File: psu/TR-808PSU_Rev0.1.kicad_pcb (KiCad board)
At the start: 2 copper layers, 142.9 x 119.4 mm, 67 parts, among them IC1 uA7805, IC2 TA7179P, P1 1, P10 10, P11 11, P12 12, P13 13, P14 14, P15 15, P16 16, P17 17, P18 18, P19 19, P2 2, P20 20, P21 21, P22 22, P3 3, P4 4, P5 5, P6 6, P7 7, P8 8, P9 9, Q1 2SB596, Q2 2SD880

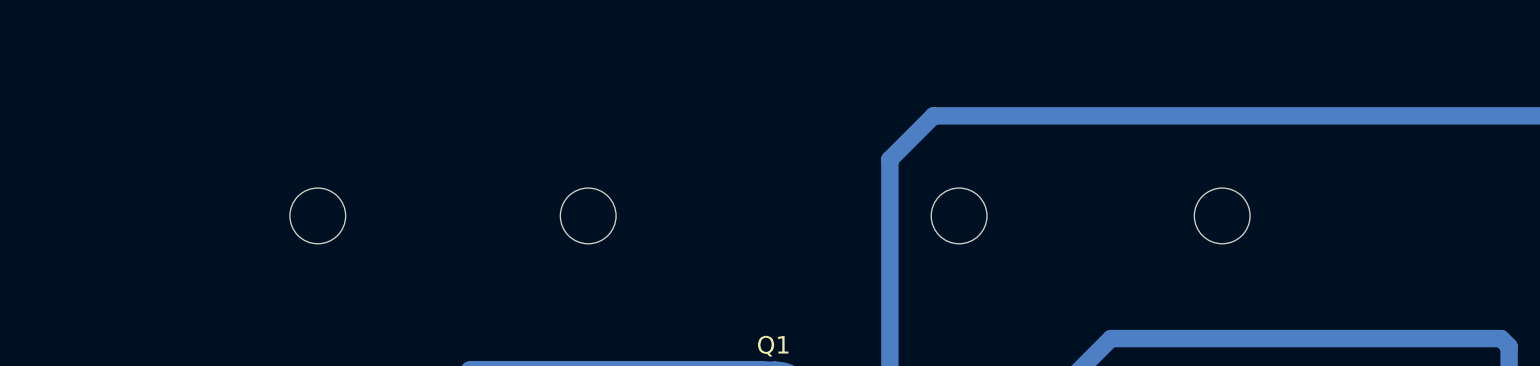
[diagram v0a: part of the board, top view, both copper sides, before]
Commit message: Schraubenloecher fuer IC1, Q1, Q2 (M3, H11-H13)
Auf der Mittelachse der Regler, 1,9 mm ueber den Seitenloechern (Bestueckungsplan).
Schaltplan mit 13 Befestigungsloechern, ERC 0, DRC 0 Fehler, Abgleich 0.

Co-Authored-By: Claude Sonnet 5.5 <noreply@anthropic.com>
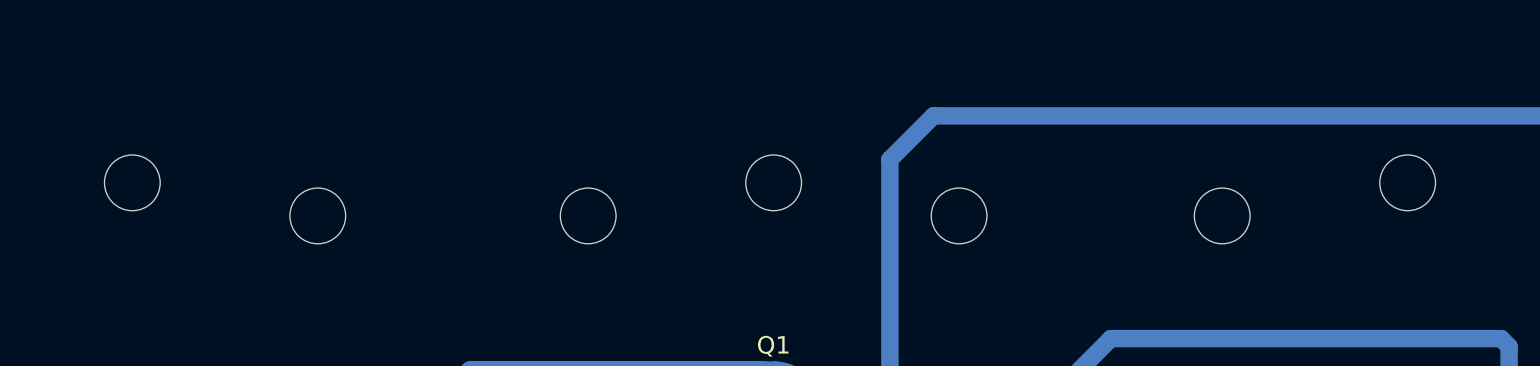
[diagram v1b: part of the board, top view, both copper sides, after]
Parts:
- added H11: M3, MountingHole:MountingHole_3.2mm_M3, F.Cu at (54.4, 32.7)
- added H12: M3, MountingHole:MountingHole_3.2mm_M3, F.Cu at (91.3, 32.7)
- added H13: M3, MountingHole:MountingHole_3.2mm_M3, F.Cu at (127.7, 32.7)

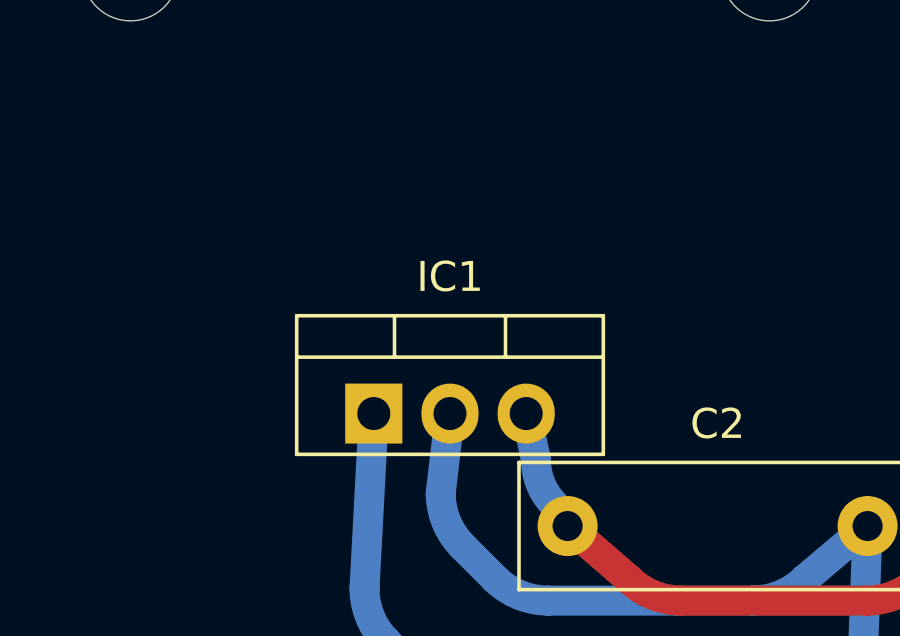
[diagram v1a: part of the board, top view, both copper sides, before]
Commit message: Regler auf einer Hoehe, Bruecken W04
IC1 auf die Hoehe von Q1/Q2 (y 47,135 mm), Bahnen ueber kurze Stuecke angebunden. D1/D2 als W04
(Platine: 2W04G; Manual W-02). Schaltplan, Stueckliste, Gerber, Ausdruck neu. ERC 0, DRC 0 Fehler, Abgleich 0.

Co-Authored-By: Claude Sonnet 5.5 <noreply@anthropic.com>
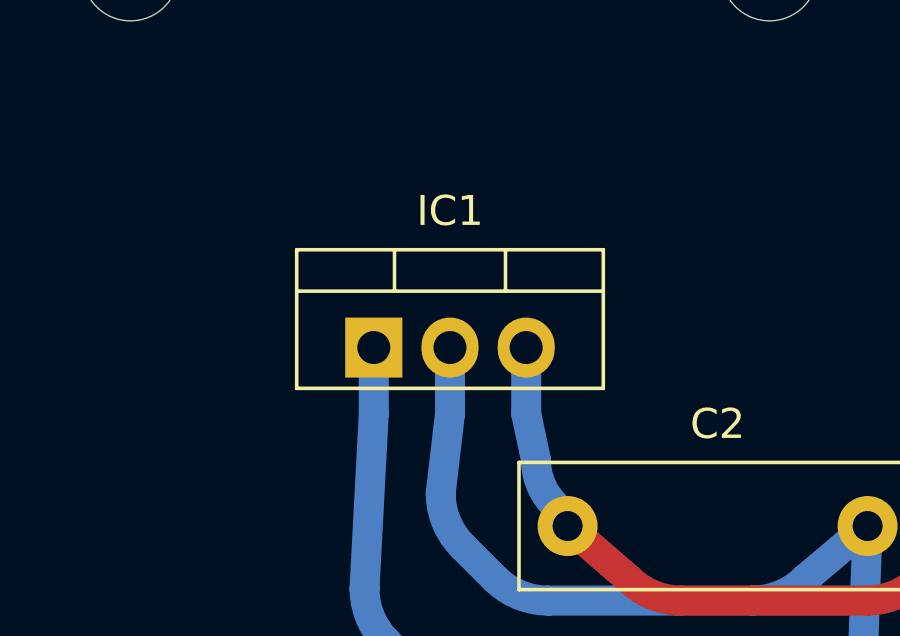
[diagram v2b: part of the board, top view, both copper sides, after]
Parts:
- D1, D2: value W02 -> W04
- moved IC1 2.20 mm to (51.9, 47.1)
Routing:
- net /GND5: track 188.5 -> 190.7 mm
- net /+5V: track 168.1 -> 170.3 mm
- net /RAW5: track 45.1 -> 47.3 mm
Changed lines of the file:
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@@
 	(footprint "Package_TO_SOT_THT:TO-220-3_Vertical"
 		(layer "F.Cu")
-		(at 51.9 49.335)
+		(at 51.9 47.135)
 		(descr "TO-220-3, Vertical, RM 2.54mm, see https://www.vishay.com/docs/66542/to-220-1.pdf")
 		(tags "TO-220-3 Vertical RM 2.54mm")
@@
 			)
 		)
-		(property "Value" "W02"
+		(property "Value" "W04"
 			(at 2.6035 8.509 0)
 			(layer "F.Fab")
@@
 			)
 		)
-		(property "Value" "W02"
+		(property "Value" "W04"
 			(at 2.6035 8.509 0)
 			(layer "F.Fab")
@@
 	)
 	(embedded_fonts no)
+	(segment
+		(start 51.9000 47.1350)
+		(end 51.9000 49.3350)
+		(width 1)
+		(layer "B.Cu")
+		(net "/RAW5")
+	)
+	(segment
+		(start 54.4400 47.1350)
+		(end 54.4400 49.3350)
+		(width 1)
+		(layer "B.Cu")
+		(net "/GND5")
+	)
+	(segment
+		(start 56.9800 47.1350)
+		(end 56.9800 49.3350)
+		(width 1)
+		(layer "B.Cu")
+		(net "/+5V")
+	)
 )
